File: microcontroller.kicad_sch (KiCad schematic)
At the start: 12 parts, among them J4 ICS-328-T, J9 PH2-06-UA, U2 ATMEGA328P-PU, Y2 ECS-160-20-4X-DU

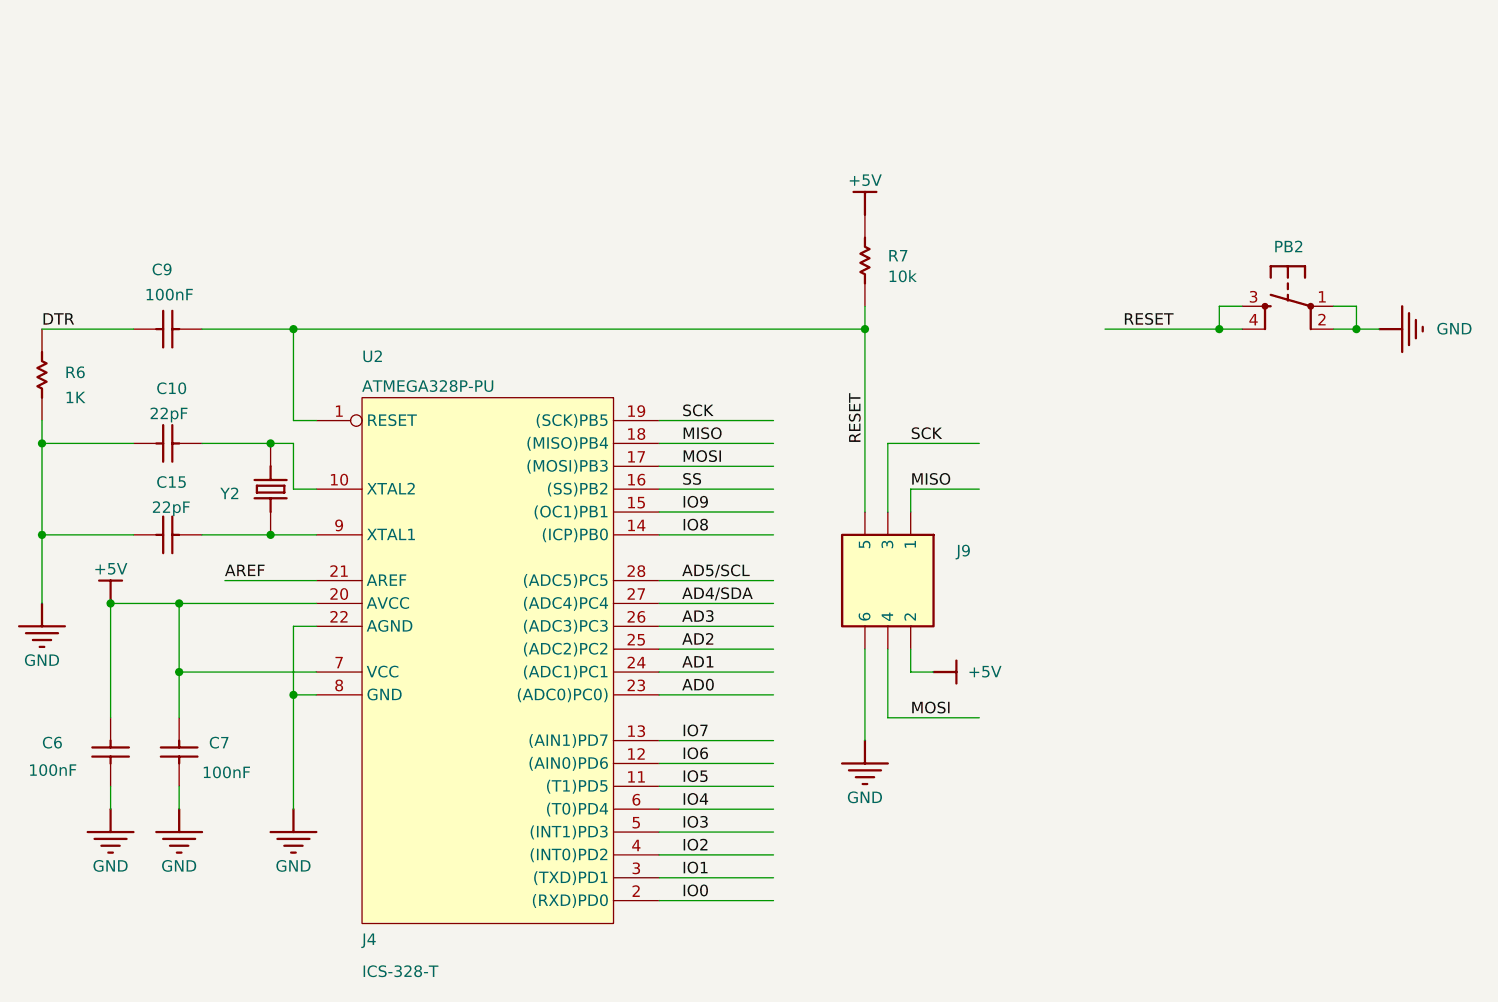
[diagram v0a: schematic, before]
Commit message: started cleanup, need to do sheet labels
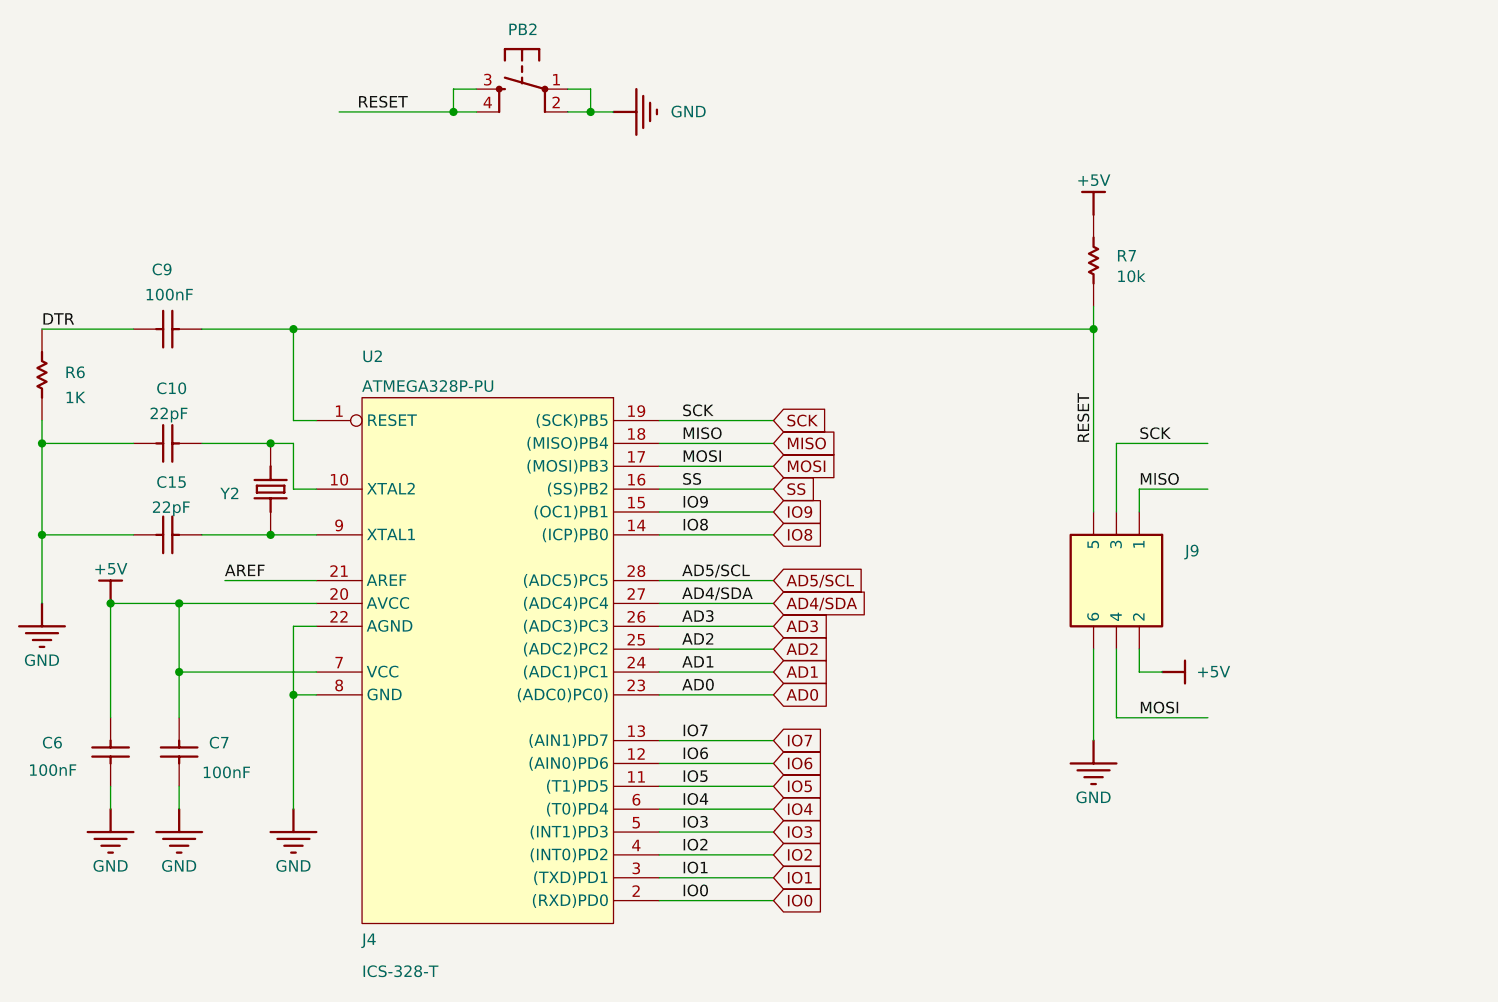
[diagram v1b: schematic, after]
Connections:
- net AD4/SDA renamed AD4/SDA
- net AD5/SCL renamed AD5/SCL
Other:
- moved on the sheet: J9, PB2, R7
